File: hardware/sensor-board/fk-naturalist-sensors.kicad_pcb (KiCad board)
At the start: 2 copper layers, 20 x 32 mm, 33 parts, among them J1 CONN_01x09, M1 FIDUCIAL, M10 FIDUCIAL, M2 FIDUCIAL, M3 MOUNT_HOLE, M4 MOUNT_HOLE, M5 FIDUCIAL, M6 FIDUCIAL, M9 FIDUCIAL, U1 MPL3115A2, U2 SHT31, U3 SPH0645, U4 TSL2591, U5 BNO055, Y1 FC-135

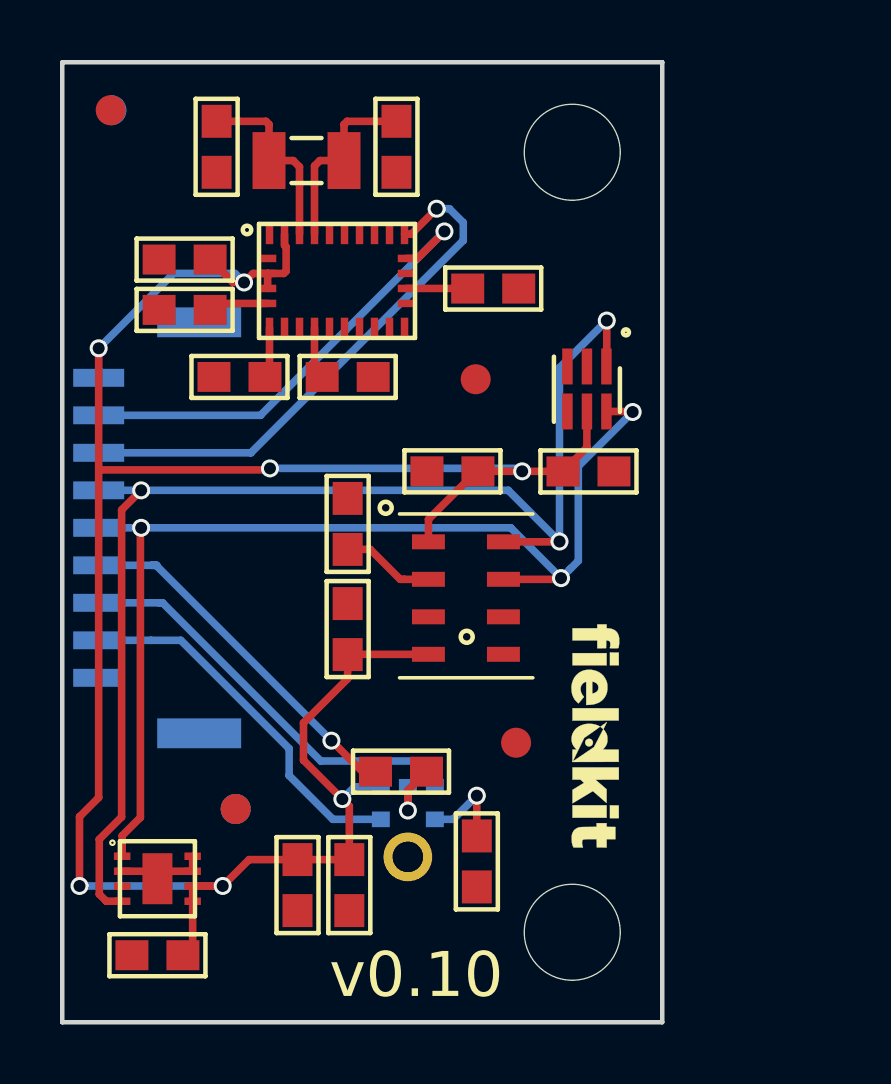
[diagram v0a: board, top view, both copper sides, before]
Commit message: Adding pullups to SDA2/SCL2.
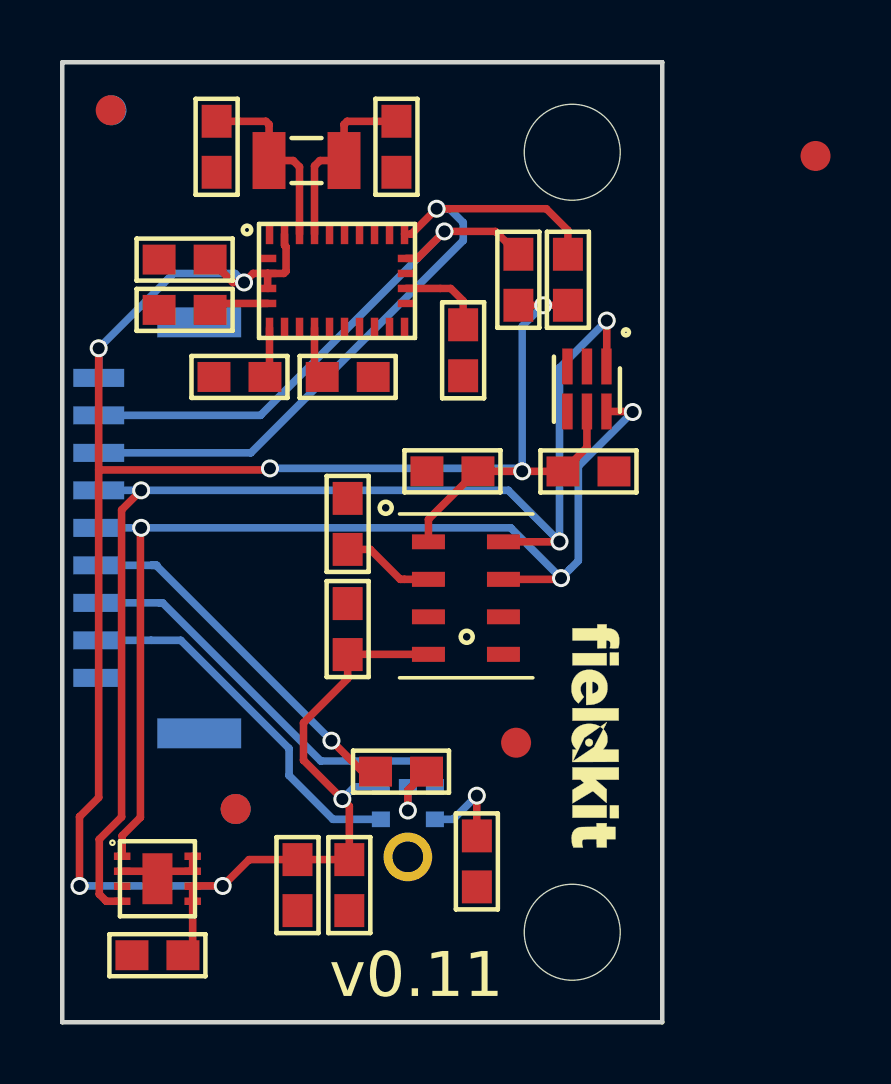
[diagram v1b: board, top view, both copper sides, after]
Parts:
- added R6: 4.7K, conservify:RES-0603, F.Cu at (236.9, 107.3)
- added R7: 4.7K, conservify:RES-0603, F.Cu at (235.2, 107.3)
- moved M1 13.6 mm to (245.1, 103.1)
- moved R3 2.29 mm to (233.4, 109.6), turned to 270 degrees
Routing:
- net 3V3: track 77.5 -> 85.2 mm, vias 7 -> 8
- net /SDA2: track 18.2 -> 23.7 mm
- net /SCL2: track 15.7 -> 18.5 mm
- net Net-(R3-Pad1): track 2.05 -> 2.86 mm
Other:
- board text added: "v0.11"
- board text removed: "v0.10"
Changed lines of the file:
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@@
-(kicad_pcb (version 20171130) (host pcbnew 5.0.0-fee4fd1~66~ubuntu16.04.1)
+(kicad_pcb (version 20171130) (host pcbnew 5.0.1-33cea8e~67~ubuntu18.04.1)
   (general
     (thickness 1.6)
     (drawings 5)
-    (tracks 168)
+    (tracks 182)
     (zones 0)
-    (modules 33)
+    (modules 35)
     (nets 34)
   )
@@
     (47 F.CrtYd user)
     (48 B.Fab user hide)
-    (49 F.Fab user)
+    (49 F.Fab user hide)
   )
   (setup
@@
     (pad_drill 0.762)
     (pad_to_mask_clearance 0.1)
+    (solder_mask_min_width 0.25)
     (aux_axis_origin 0 0)
     (visible_elements FFFFFF7F)
@@
   )
   (module conservify:RES-0603 (layer F.Cu)
-    (at 234.3658 107.5436)
+    (at 233.3625 109.601 270)
     (descr "Capacitor SMD 0603")
     (tags "capacitor 0603")
     (attr smd)
-    (fp_text reference R3 (at 0 -1.5748) (layer F.SilkS) hide
-      (effects (font (size 1 1) (thickness 0.15)))
-    )
-    (fp_text value 10K (at 3.2342 -0.1436) (layer F.Fab)
+    (fp_text reference R3 (at 0 -1.5748 270) (layer F.SilkS) hide
+      (effects (font (size 1 1) (thickness 0.15)))
+    )
+    (fp_text value 10K (at 3.2342 -0.1436 270) (layer F.Fab)
       (effects (font (size 1 1) (thickness 0.15)))
     )
@@
     (fp_line (start -1.6 -0.7) (end 1.6 -0.7) (layer F.SilkS) (width 0.15))
     (fp_line (start 1.6 0.7) (end -1.6 0.7) (layer F.SilkS) (width 0.15))
-    (pad 1 smd rect (at -0.85 0) (size 1.1 1) (layers F.Cu F.Paste F.Mask)
+    (pad 1 smd rect (at -0.85 0 270) (size 1.1 1) (layers F.Cu F.Paste F.Mask)
       (net 23 "Net-(R3-Pad1)"))
-    (pad 2 smd rect (at 0.85 0) (size 1.1 1) (layers F.Cu F.Paste F.Mask)
+    (pad 2 smd rect (at 0.85 0 270) (size 1.1 1) (layers F.Cu F.Paste F.Mask)
       (net 2 GND))
   )
@@
   )
   (module conservify:FIDUCIAL-1MM (layer F.Cu)
-    (at 233.7816 110.5662)
+    (at 245.11 103.124)
     (descr "Circular Fiducial, 1mm bare copper top; 2.54mm keepout")
     (tags marker)
@@
       (net 33 "Net-(M2-Pad~)") (solder_mask_margin 0.5) (clearance 0.5))
   )
-  (gr_text v0.10 (at 231.8004 130.429) (layer F.SilkS)
+  (module conservify:RES-0603 (layer F.Cu)
+    (at 236.855 107.2515 270)
+    (descr "Capacitor SMD 0603")
+    (tags "capacitor 0603")
+    (attr smd)
+    (fp_text reference R6 (at 0 -1.5748 270) (layer F.SilkS) hide
+      (effects (font (size 1 1) (thickness 0.15)))
+    )
+    (fp_text value 4.7K (at 0 -0.0635 270) (layer F.Fab)
+      (effects (font (size 1 1) (thickness 0.15)))
+    )
+    (fp_line (start 1.6 0.7) (end -1.6 0.7) (layer F.SilkS) (width 0.15))
+    (fp_line (start -1.6 -0.7) (end 1.6 -0.7) (layer F.SilkS) (width 0.15))
+    (fp_line (start 1.6 -0.7) (end 1.6 0.7) (layer F.SilkS) (width 0.15))
+    (fp_line (start -1.6 -0.7) (end -1.6 0.7) (layer F.SilkS) (width 0.15))
+    (fp_line (start 1.65 -0.75) (end -1.65 -0.75) (layer F.CrtYd) (width 0.05))
+    (fp_line (start 1.65 0.75) (end 1.65 -0.75) (layer F.CrtYd) (width 0.05))
+    (fp_line (start -1.65 0.75) (end 1.65 0.75) (layer F.CrtYd) (width 0.05))
+    (fp_line (start -1.65 -0.75) (end -1.65 0.75) (layer F.CrtYd) (width 0.05))
+    (pad 2 smd rect (at 0.85 0 270) (size 1.1 1) (layers F.Cu F.Paste F.Mask)
+      (net 3 3V3))
+    (pad 1 smd rect (at -0.85 0 270) (size 1.1 1) (layers F.Cu F.Paste F.Mask)
+      (net 26 /SDA2))
+  )
+  (module conservify:RES-0603 (layer F.Cu)
+    (at 235.204 107.2515 270)
+    (descr "Capacitor SMD 0603")
+    (tags "capacitor 0603")
+    (attr smd)
+    (fp_text reference R7 (at 0 -1.5748 270) (layer F.SilkS) hide
+      (effects (font (size 1 1) (thickness 0.15)))
+    )
+    (fp_text value 4.7K (at 0.0635 -0.0635 270) (layer F.Fab)
+      (effects (font (size 1 1) (thickness 0.15)))
+    )
+    (fp_line (start -1.65 -0.75) (end -1.65 0.75) (layer F.CrtYd) (width 0.05))
+    (fp_line (start -1.65 0.75) (end 1.65 0.75) (layer F.CrtYd) (width 0.05))
+    (fp_line (start 1.65 0.75) (end 1.65 -0.75) (layer F.CrtYd) (width 0.05))
+    (fp_line (start 1.65 -0.75) (end -1.65 -0.75) (layer F.CrtYd) (width 0.05))
+    (fp_line (start -1.6 -0.7) (end -1.6 0.7) (layer F.SilkS) (width 0.15))
+    (fp_line (start 1.6 -0.7) (end 1.6 0.7) (layer F.SilkS) (width 0.15))
+    (fp_line (start -1.6 -0.7) (end 1.6 -0.7) (layer F.SilkS) (width 0.15))
+    (fp_line (start 1.6 0.7) (end -1.6 0.7) (layer F.SilkS) (width 0.15))
+    (pad 1 smd rect (at -0.85 0 270) (size 1.1 1) (layers F.Cu F.Paste F.Mask)
+      (net 31 /SCL2))
+    (pad 2 smd rect (at 0.85 0 270) (size 1.1 1) (layers F.Cu F.Paste F.Mask)
+      (net 3 3V3))
+  )
+  (gr_text v0.11 (at 231.8004 130.429) (layer F.SilkS)
     (effects (font (size 1.5 1.5) (thickness 0.3)))
   )
@@
   (segment (start 226.9236 113.538) (end 235.233 113.538) (width 0.254) (layer B.Cu) (net 3))
   (segment (start 235.233 113.538) (end 235.331 113.636) (width 0.254) (layer B.Cu) (net 3))
+  (segment (start 235.331 108.2285) (end 235.204 108.1015) (width 0.25) (layer F.Cu) (net 3))
+  (via (at 236.0295 108.1015) (size 0.6) (drill 0.4) (layers F.Cu B.Cu) (net 3))
+  (segment (start 235.331 108.8) (end 236.0295 108.1015) (width 0.25) (layer B.Cu) (net 3))
+  (segment (start 235.331 113.636) (end 235.331 108.8) (width 0.25) (layer B.Cu) (net 3))
+  (segment (start 235.204 108.1015) (end 236.0295 108.1015) (width 0.25) (layer F.Cu) (net 3))
+  (segment (start 236.0295 108.1015) (end 236.855 108.1015) (width 0.25) (layer F.Cu) (net 3))
   (via (at 233.818854 124.447354) (size 0.6) (drill 0.4) (layers F.Cu B.Cu) (net 4))
   (segment (start 233.818854 124.447354) (end 233.818854 125.786733) (width 0.254) (layer F.Cu) (net 4))
@@
   (segment (start 229.3928 102.0724) (end 229.496 101.9692) (width 0.254) (layer F.Cu) (net 22))
   (segment (start 229.3928 103.2764) (end 229.3928 102.0724) (width 0.254) (layer F.Cu) (net 22))
-  (segment (start 233.5118 107.5396) (end 233.5158 107.5436) (width 0.254) (layer F.Cu) (net 23))
-  (segment (start 231.4713 107.5396) (end 233.5118 107.5396) (width 0.254) (layer F.Cu) (net 23))
+  (segment (start 233.3625 107.951) (end 232.9511 107.5396) (width 0.25) (layer F.Cu) (net 23))
+  (segment (start 232.9511 107.5396) (end 232.6005 107.5396) (width 0.25) (layer F.Cu) (net 23))
+  (segment (start 233.3625 108.751) (end 233.3625 107.951) (width 0.25) (layer F.Cu) (net 23))
+  (segment (start 231.4713 107.5396) (end 232.6005 107.5396) (width 0.254) (layer F.Cu) (net 23))
   (segment (start 226.9088 110.3388) (end 226.7576 110.49) (width 0.254) (layer F.Cu) (net 24))
   (segment (start 226.9088 108.8521) (end 226.9088 110.3388) (width 0.254) (layer F.Cu) (net 24))
@@
   (segment (start 226.287562 113.0192) (end 233.367201 105.939561) (width 0.254) (layer B.Cu) (net 26))
   (segment (start 221.2144 113.0192) (end 226.287562 113.0192) (width 0.254) (layer B.Cu) (net 26))
+  (segment (start 232.903671 104.8823) (end 232.479407 104.8823) (width 0.25) (layer F.Cu) (net 26))
+  (segment (start 236.855 106.4015) (end 236.855 105.6015) (width 0.25) (layer F.Cu) (net 26))
+  (segment (start 236.855 105.6015) (end 236.1358 104.8823) (width 0.25) (layer F.Cu) (net 26))
+  (segment (start 236.1358 104.8823) (end 232.903671 104.8823) (width 0.25) (layer F.Cu) (net 26))
   (via (at 232.7402 105.6386) (size 0.6) (drill 0.4) (layers F.Cu B.Cu) (net 31))
   (segment (start 231.8392 106.5396) (end 232.7402 105.6386) (width 0.254) (layer F.Cu) (net 31))
@@
   (segment (start 226.6096 111.7692) (end 232.7402 105.6386) (width 0.254) (layer B.Cu) (net 31))
   (segment (start 221.2144 111.7692) (end 226.6096 111.7692) (width 0.254) (layer B.Cu) (net 31))
+  (segment (start 234.4411 105.6386) (end 235.204 106.4015) (width 0.25) (layer F.Cu) (net 31))
+  (segment (start 232.7402 105.6386) (end 234.4411 105.6386) (width 0.25) (layer F.Cu) (net 31))
   (zone (net 2) (net_name GND) (layer B.Cu) (hatch edge 0.508)
     (connect_pads (clearance 0.3))
     (min_thickness 0.2032)
-    (fill (arc_segments 32) (thermal_gap 0.3) (thermal_bridge_width 0.254))
+    (fill yes (arc_segments 32) (thermal_gap 0.3) (thermal_bridge_width 0.254))
     (polygon
       (pts
@@
     (connect_pads (clearance 0.2032))
     (min_thickness 0.2032)
-    (fill (arc_segments 32) (thermal_gap 0.254) (thermal_bridge_width 0.254))
+    (fill yes (arc_segments 32) (thermal_gap 0.254) (thermal_bridge_width 0.254))
     (polygon
       (pts

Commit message: Fix location of a fudicial.
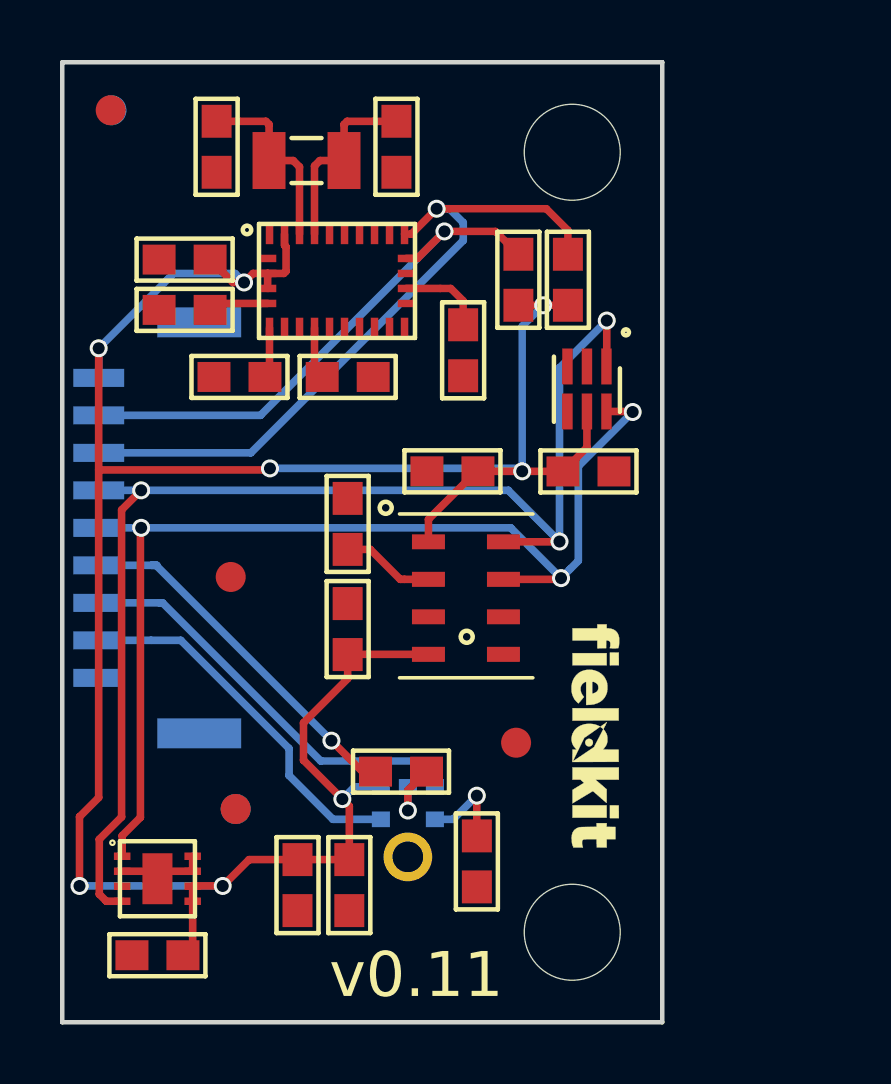
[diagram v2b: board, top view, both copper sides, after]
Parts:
- moved M1 24.0 mm to (225.6, 117.2)
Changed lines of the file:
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@@
   )
   (module conservify:FIDUCIAL-1MM (layer F.Cu)
-    (at 245.11 103.124)
+    (at 225.6155 117.1575)
     (descr "Circular Fiducial, 1mm bare copper top; 2.54mm keepout")
     (tags marker)
@@
     (connect_pads (clearance 0.3))
     (min_thickness 0.2032)
-    (fill yes (arc_segments 32) (thermal_gap 0.3) (thermal_bridge_width 0.254))
+    (fill (arc_segments 32) (thermal_gap 0.3) (thermal_bridge_width 0.254))
     (polygon
       (pts
@@
     (connect_pads (clearance 0.2032))
     (min_thickness 0.2032)
-    (fill yes (arc_segments 32) (thermal_gap 0.254) (thermal_bridge_width 0.254))
+    (fill (arc_segments 32) (thermal_gap 0.254) (thermal_bridge_width 0.254))
     (polygon
       (pts

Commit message: Standardized hole diameters, pushed connector away from board edge, and panelized for production.
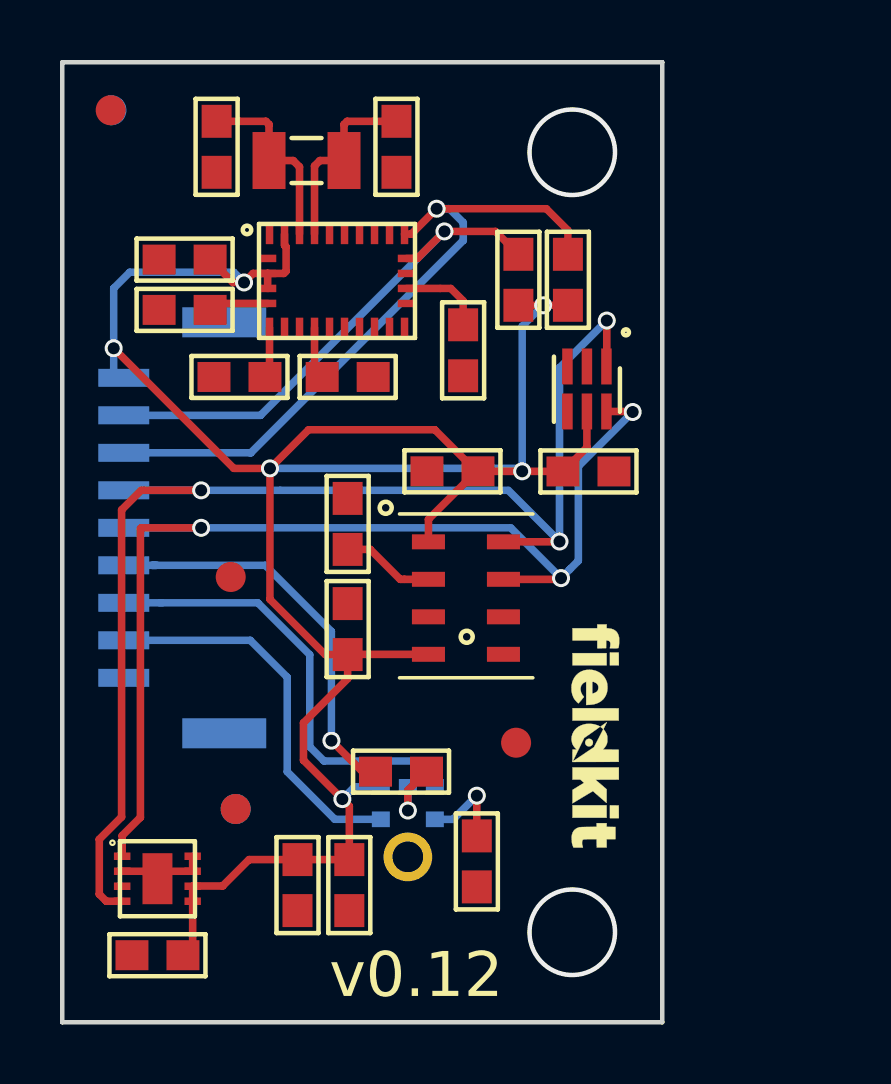
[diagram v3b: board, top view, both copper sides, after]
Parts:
- removed M3, M4: MOUNT_HOLE, conservify:HOLE_NPTH_3.2MM
- moved J1 0.84 mm to (224.0, 115.5)
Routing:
- net 3V3: track 85.2 -> 79.8 mm, vias 8 -> 6
- net /I2S_DATA: track 12.2 -> 13.7 mm
- net /I2S_WS: track 14.0 -> 15.1 mm
- net /SDA: track 36.7 -> 37.7 mm
- net /SCL2: track 18.5 -> 17.5 mm
- net /SCL: track 42.4 -> 43.4 mm
- net /SDA2: track 23.7 -> 22.7 mm
- net (no net): vias 0 -> 2
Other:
- board text added: "v0.12"
- board text removed: "v0.11"
